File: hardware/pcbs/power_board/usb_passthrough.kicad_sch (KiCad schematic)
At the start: 3 parts, among them J3 USB3_B_Micro, J4 USB3_A

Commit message: power_board: update components to new versions and annotate
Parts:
- J3: Part (none) -> GSB343K33AHR
- J4: Part (none) -> GSB3116344KHHR
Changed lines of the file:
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@@
+			)
+		)
+		(property "Part" "GSB343K33AHR"
+			(at 140.97 95.25 0)
+			(effects
+				(font
+					(size 1.27 1.27)
+				)
+				(hide yes)
 			)
 		)
@@
 		(dnp no)
 		(fields_autoplaced yes)
-		(property "Reference" "#PWR08"
+		(property "Reference" "#PWR07"
 			(at 138.43 123.19 0)
 			(effects
@@
 			(project "power_board"
 				(path "/4b166175-80a4-48c6-994d-6e62a6160b87/91441b40-0438-4eff-8649-c295c7239fb6"
-					(reference "#PWR08")
+					(reference "#PWR07")
 					(unit 1)
 				)
@@
 		(dnp no)
 		(fields_autoplaced yes)
-		(property "Reference" "#PWR010"
+		(property "Reference" "#PWR09"
 			(at 190.5 123.19 0)
 			(effects
@@
 			(project "power_board"
 				(path "/4b166175-80a4-48c6-994d-6e62a6160b87/91441b40-0438-4eff-8649-c295c7239fb6"
-					(reference "#PWR010")
+					(reference "#PWR09")
 					(unit 1)
 				)
@@
 			)
 		)
+		(property "Part" "GSB3116344KHHR "
+			(at 187.96 95.25 0)
+			(effects
+				(font
+					(size 1.27 1.27)
+				)
+				(hide yes)
+			)
+		)
 		(pin "9"
 		)
@@
 		(dnp no)
 		(fields_autoplaced yes)
-		(property "Reference" "#PWR09"
+		(property "Reference" "#PWR08"
 			(at 163.83 92.71 0)
 			(effects
@@
 			(project "power_board"
 				(path "/4b166175-80a4-48c6-994d-6e62a6160b87/91441b40-0438-4eff-8649-c295c7239fb6"
-					(reference "#PWR09")
-					(unit 1)
-				)
+					(reference "#PWR08")
+					(unit 1)
+				)

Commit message: audio_board, power_board: update shop and part links
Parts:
- C1: Part (none) -> C 1μF 16V 0805
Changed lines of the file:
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@@
+			)
+		)
+		(property "Part" "C 1μF 16V 0805"
+			(at 163.83 78.74 0)
+			(effects
+				(font
+					(size 1.27 1.27)
+				)
+				(hide yes)
 			)
 		)

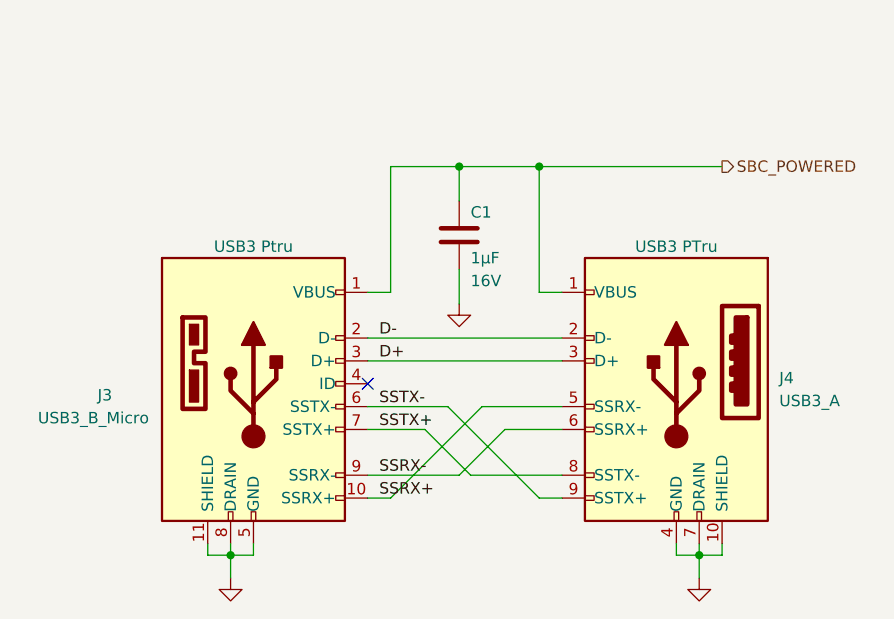
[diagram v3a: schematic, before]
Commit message: power_board: final-ish shape
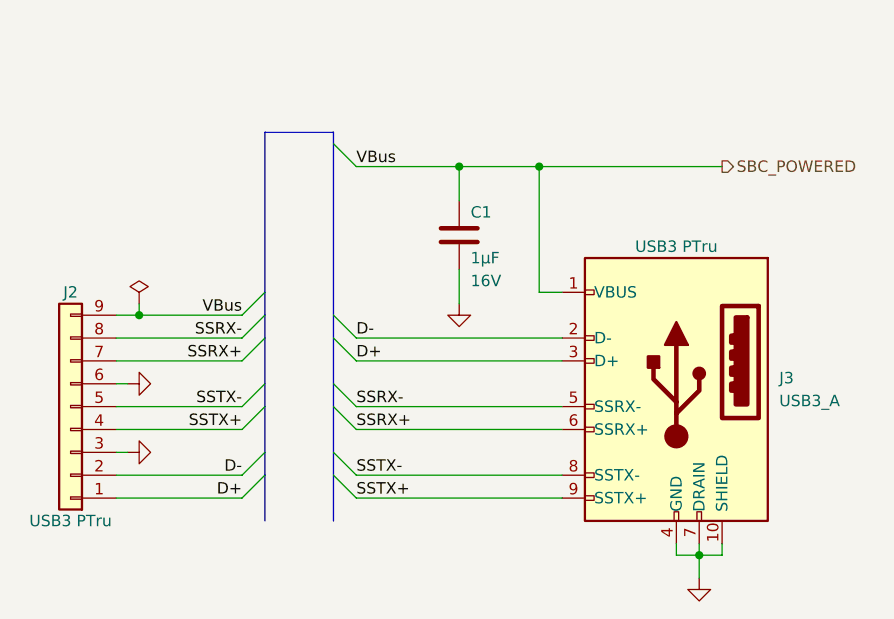
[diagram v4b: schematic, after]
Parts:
- removed J3: USB3_B_Micro, Connector_USB:USB3_Micro-B_Connfly_DS1104-01, symbol conn:USB3_B_Micro_PassiveGND
- added J2: MTA100_9, Connector_MTA-100:mta100_01x9_P2.54_647050-9, symbol Connector_Generic:Conn_01x09
- renumbered J4 to J3
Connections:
- net D+: now also J2.1 (Pin_1)
- net D-: now also J2.2 (Pin_2)
- net GND: now also J2.3 (Pin_3), J2.6 (Pin_6)
- net SBC_POWERED: now also J2.9 (Pin_9)
- net SSRX+: now also J3.6 (SSRX+), J2.7 (Pin_7); no longer J3.5 (SSRX-)
- net SSRX-: now also J3.5 (SSRX-), J2.8 (Pin_8); no longer J3.6 (SSRX+)
- net SSTX+: now also J3.9 (SSTX+), J2.4 (Pin_4); no longer J3.8 (SSTX-)
- net SSTX-: now also J3.8 (SSTX-), J2.5 (Pin_5); no longer J3.9 (SSTX+)
- no-connect marks 1 -> 0

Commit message: power_board: final touches
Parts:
- J2: Part (none) -> 640456-9; Shop (none) -> https://eu.mouser.com/ProductDetail/TE-Connectivity-AMP/640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
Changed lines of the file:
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@@
+			)
+		)
+		(property "Part" "640456-9"
+			(at 120.65 97.79 0)
+			(effects
+				(font
+					(size 1.27 1.27)
+				)
+				(hide yes)
+			)
+		)
+		(property "Shop" "https://eu.mouser.com/ProductDetail/TE-Connectivity-AMP/640456-9?qs=%2F35zJ5USjokUKOCQQwb90w%3D%3D"
+			(at 120.65 97.79 0)
+			(effects
+				(font
+					(size 1.27 1.27)
+				)
+				(hide yes)
 			)
 		)

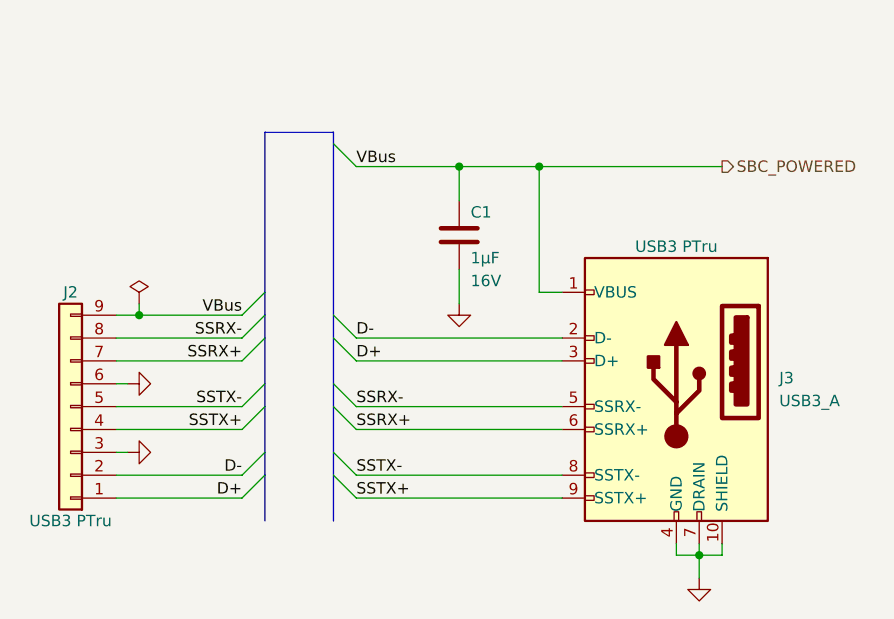
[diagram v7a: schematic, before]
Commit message: power_board: use USB3-A passthrough connector and fix chg EN
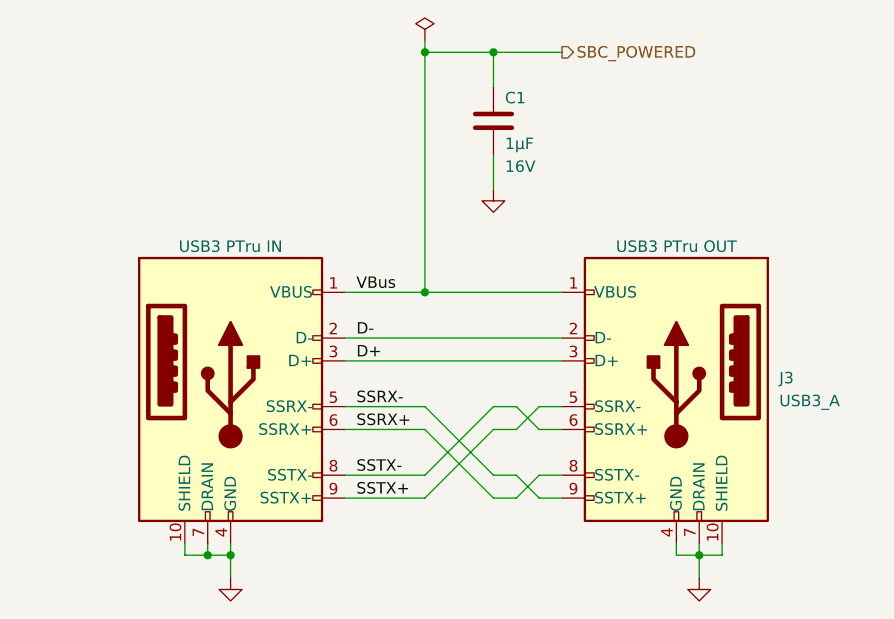
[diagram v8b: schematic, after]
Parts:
- removed J2: MTA100_9, Connector_MTA-100:mta100_01x9_P2.54_647050-9, symbol Connector_Generic:Conn_01x09
- added J2: USB3_A, conn:USB3_A_Amphenol_GSB3116344KHHR, symbol Connector:USB3_A
- J3: Purpose USB3 PTru -> USB3 PTru OUT
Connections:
- net D+: now also J2.3 (D+)
- net D-: now also J2.2 (D-)
- net GND: now also J2.10 (SHIELD), J2.4 (GND), J2.7 (DRAIN)
- net SBC_POWERED: now also J2.1 (VBUS)
- net SSRX+: now also J3.8 (SSTX-), J2.6 (SSRX+); no longer J3.6 (SSRX+)
- net SSRX-: now also J3.9 (SSTX+), J2.5 (SSRX-); no longer J3.5 (SSRX-)
- net SSTX+: now also J3.5 (SSRX-), J2.9 (SSTX+); no longer J3.9 (SSTX+)
- net SSTX-: now also J3.6 (SSRX+), J2.8 (SSTX-); no longer J3.8 (SSTX-)
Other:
- moved on the sheet: C1
